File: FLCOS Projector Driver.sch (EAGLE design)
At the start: 67 parts, among them IC1 LM1117MPX-3.3, IC2 MIC5323-1.8YD5-TR, IC3 MIC5504-2.5YM5-TR, IC4 TVP5150-NTSC_DECODER, IC5 CH340G, IC6 ESP32-WROOM-32U, IC7 LM3414, IC8 LM3414, IC9 LM3414, J1 MEM2075-00-140-01-A, T1 S8050, T2 S8050, X1 14.31818MHz, X2 12MHz

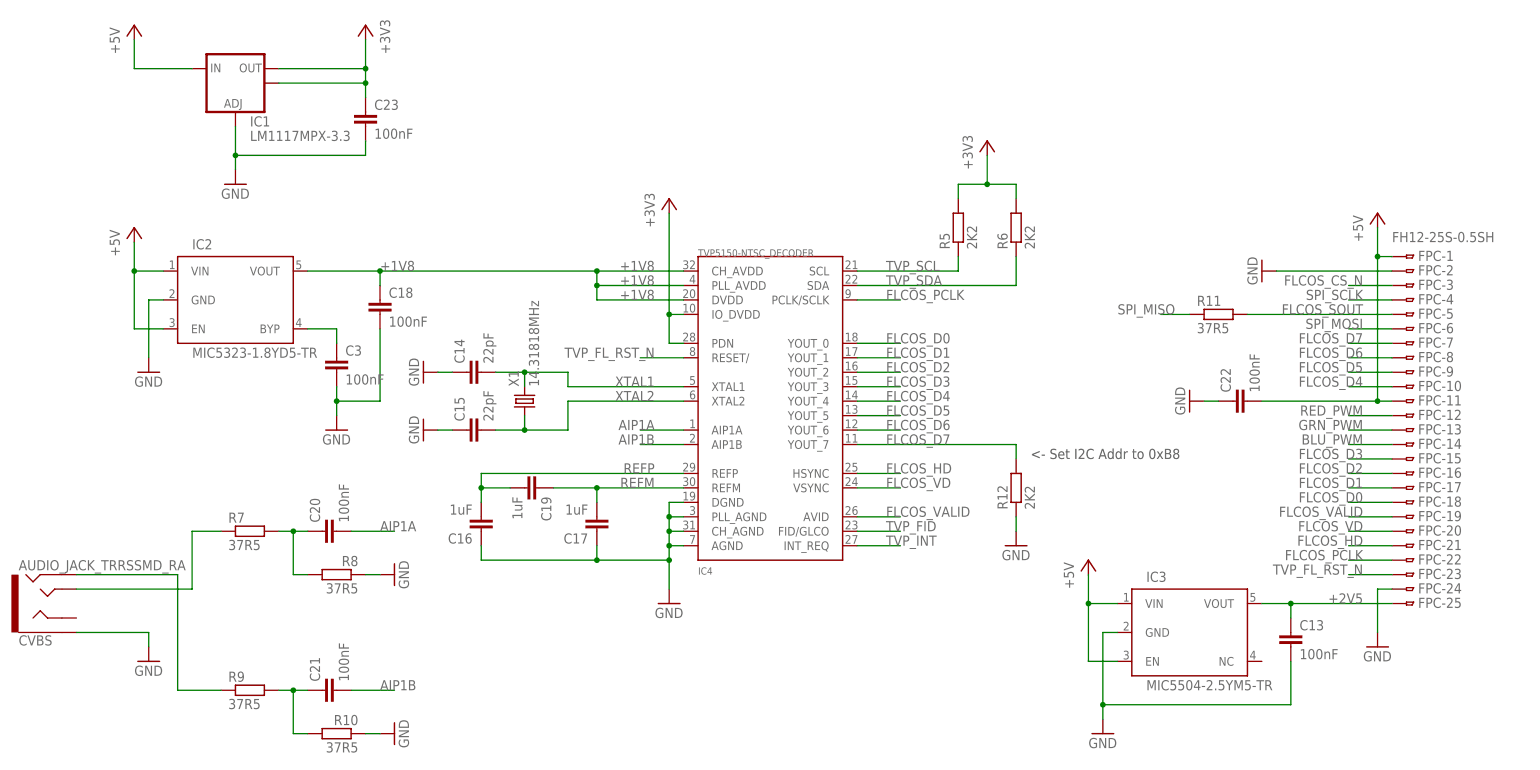
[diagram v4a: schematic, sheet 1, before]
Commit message: XLSX BOM finished. Tweaked FLCOS mounting points
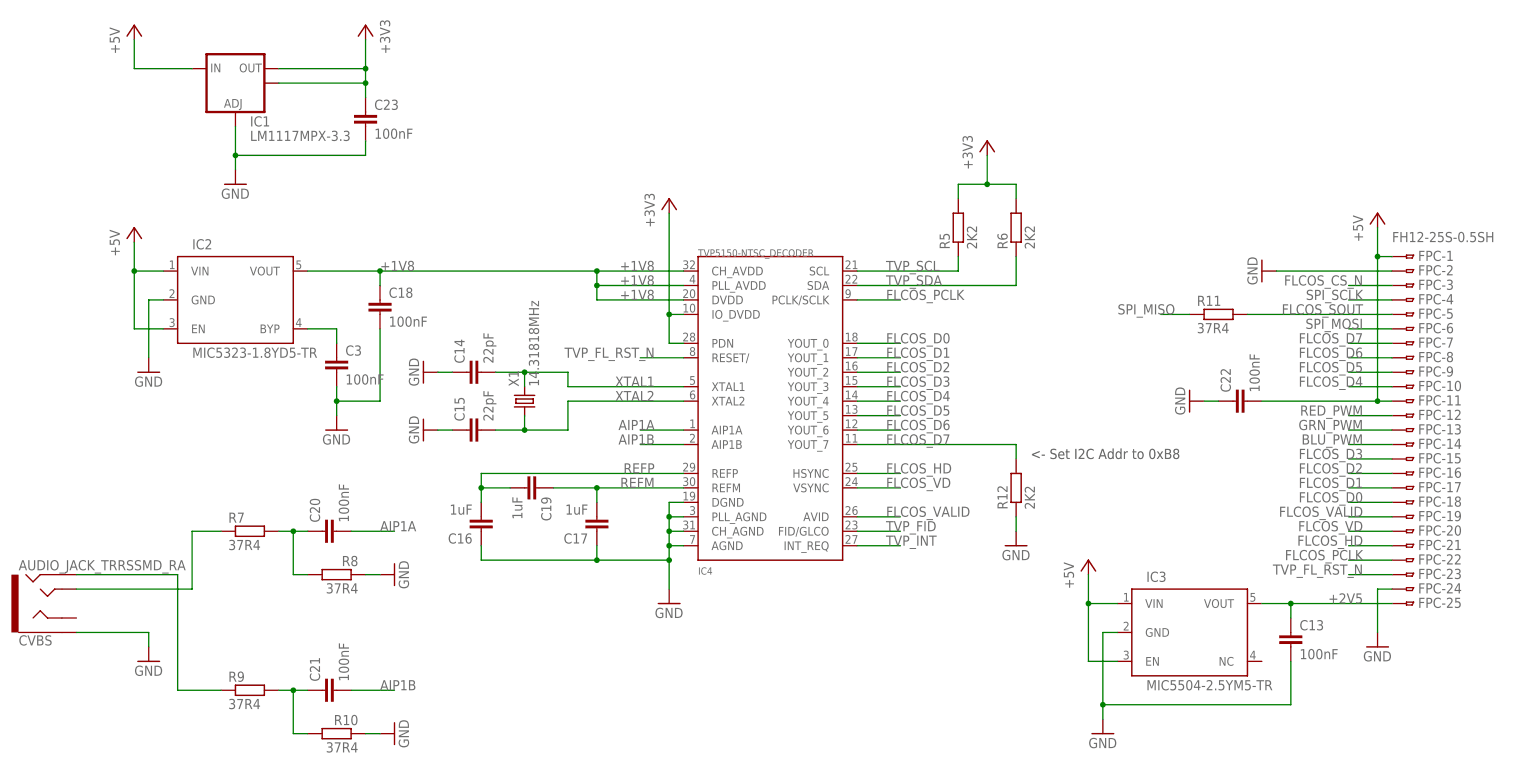
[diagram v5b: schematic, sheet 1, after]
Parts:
- R1, R15, R3: value 80K -> 82K
- R10, R11, R7, R8, R9: value 37R5 -> 37R4
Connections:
- net N$27: now also D2.A; no longer D3.A
- net N$9: now also D3.A; no longer D2.A
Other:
- moved on the sheet: D2, D3

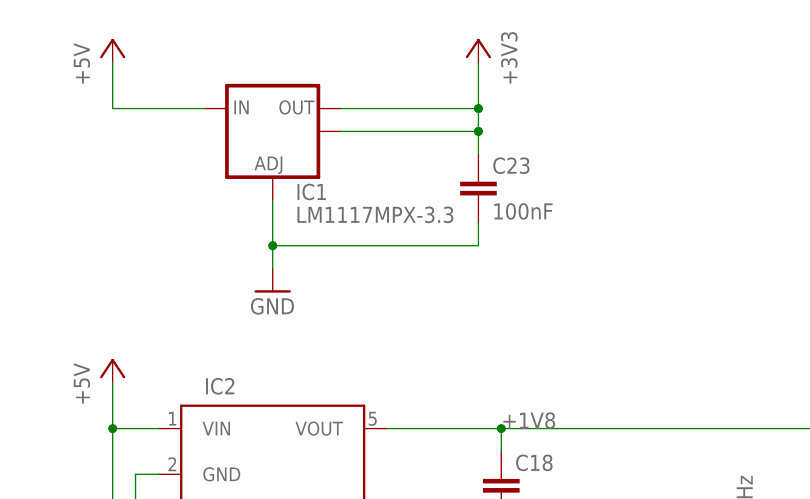
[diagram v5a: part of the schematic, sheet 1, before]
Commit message: Added Mouser cart XLS. BOM tweaks due to low stocks
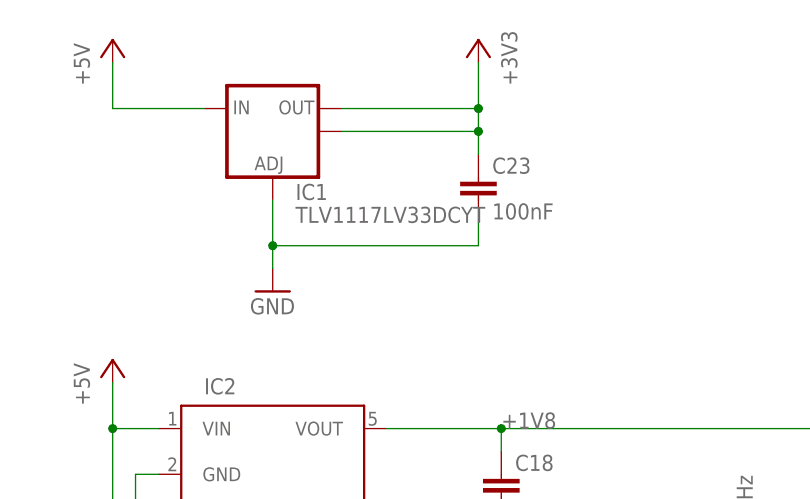
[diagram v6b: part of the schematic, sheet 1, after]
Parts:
- IC1: value LM1117MPX-3.3 -> TLV1117LV33DCYT
- IC6: value ESP32-WROOM-32U -> ESP32-WROOM-32UE-N4
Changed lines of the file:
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@@
 <part name="GND65" library="supply1" deviceset="GND" device=""/>
 <part name="U$43" library="supply1" deviceset="+3V3" device=""/>
-<part name="IC6" library="ESP32-WROOM-32U" deviceset="ESP32-WROOM-32U" device=""/>
+<part name="IC6" library="ESP32-WROOM-32U" deviceset="ESP32-WROOM-32U" device="" value="ESP32-WROOM-32UE-N4"/>
 <part name="GND66" library="supply1" deviceset="GND" device=""/>
 <part name="GND67" library="supply1" deviceset="GND" device=""/>
@@
 <part name="P+8" library="supply1" deviceset="+5V" device=""/>
 <part name="P+9" library="supply1" deviceset="+5V" device=""/>
-<part name="IC1" library="SparkFun" deviceset="V_REG_LM1117" device="SOT223" value="LM1117MPX-3.3"/>
+<part name="IC1" library="SparkFun" deviceset="V_REG_LM1117" device="SOT223" value="TLV1117LV33DCYT"/>
 <part name="RGB" library="con-jst" deviceset="ZH-8" device=""/>
 <part name="L2" library="A_butts" deviceset="INDUCTOR" device="-TAIYO-YUDEN-6X2.8" value="15uH"/>

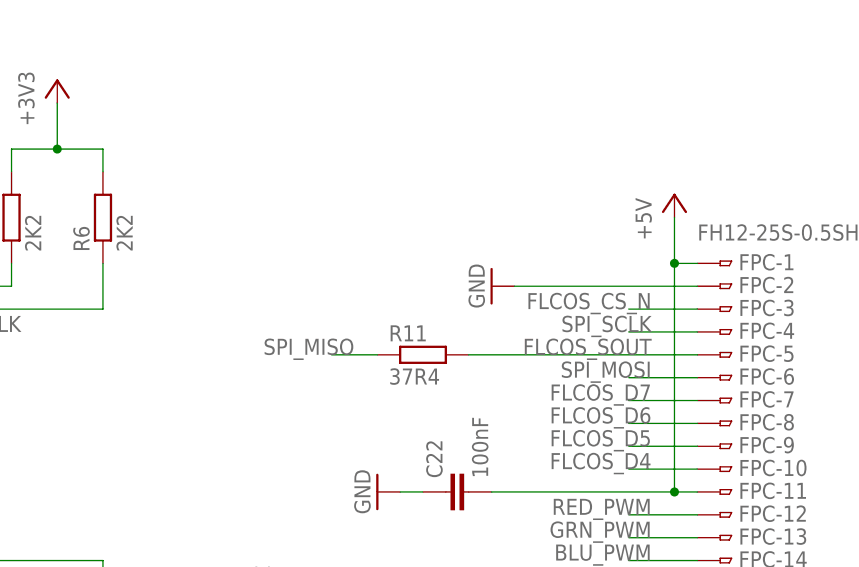
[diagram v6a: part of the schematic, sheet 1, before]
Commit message: Changed R11 to a pull-up for FLCOS_SOUT
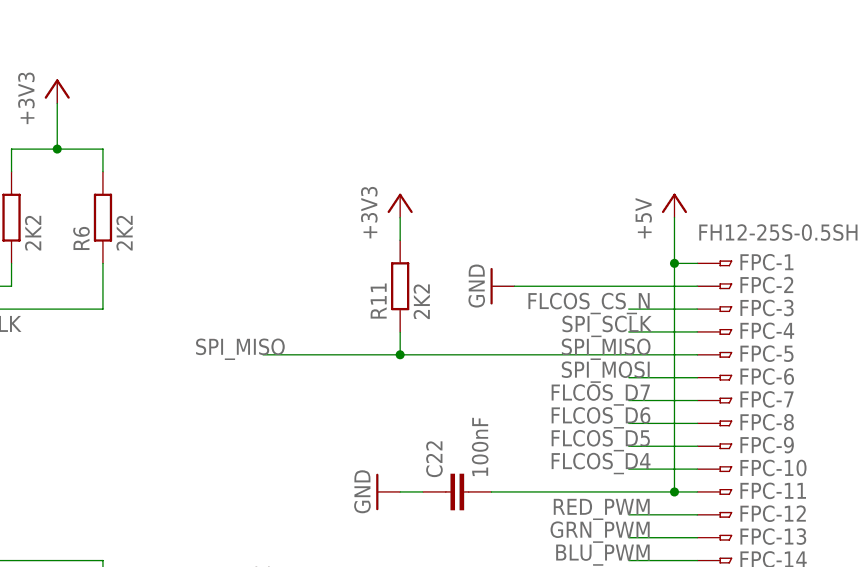
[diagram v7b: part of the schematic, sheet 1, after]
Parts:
- R11: value 37R4 -> 2K2
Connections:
- removed net FLCOS_SOUT: FPC-5.1, R11.2
- net +3V3: now also R11.2
- net SPI_MISO: now also FPC-5.1
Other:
- moved on the sheet: R11
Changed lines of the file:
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@@
 <part name="P+12" library="supply1" deviceset="+5V" device=""/>
 <part name="+3V3" library="supply1" deviceset="+3V3" device=""/>
-<part name="R11" library="rcl" deviceset="R-EU_" device="R0603" value="37R4"/>
 <part name="R5" library="rcl" deviceset="R-EU_" device="R0603" value="2K2"/>
 <part name="R6" library="rcl" deviceset="R-EU_" device="R0603" value="2K2"/>
@@
 <part name="R16" library="rcl" deviceset="R-EU_" device="R0603" value="22K"/>
 <part name="CVBS" library="SparkFun-Connectors" deviceset="AUDIO_JACK_TRRS" device="SMD_RA"/>
+<part name="R11" library="rcl" deviceset="R-EU_" device="R0603" value="2K2"/>
+<part name="+3V4" library="supply1" deviceset="+3V3" device=""/>
 </parts>
 <sheets>
@@
 <instance part="IC1" gate="G$1" x="-43.18" y="111.76"/>
 <instance part="+3V3" gate="G$1" x="88.9" y="99.06"/>
-<instance part="R11" gate="G$1" x="129.54" y="68.58"/>
 <instance part="R5" gate="G$1" x="83.82" y="83.82" rot="R90"/>
 <instance part="R6" gate="G$1" x="93.98" y="83.82" rot="R90"/>
@@
 <instance part="C3" gate="G$1" x="-25.4" y="60.96"/>
 <instance part="CVBS" gate="G$1" x="-76.2" y="17.78" rot="MR180"/>
+<instance part="R11" gate="G$1" x="127" y="76.2" rot="R90"/>
+<instance part="+3V4" gate="G$1" x="127" y="86.36"/>
 </instances>
 <busses>
@@
 </segment>
 </net>
-<net name="FLCOS_SOUT" class="0">
-<segment>
-<pinref part="FPC" gate="-5" pin="1"/>
-<label x="154.94" y="68.58" size="1.778" layer="95" rot="MR0"/>
-<wire x1="160.02" y1="68.58" x2="134.62" y2="68.58" width="0.1524" layer="91"/>
-<pinref part="R11" gate="G$1" pin="2"/>
-</segment>
-</net>
 <net name="SPI_MOSI" class="0">
 <segment>
@@
 <pinref part="R6" gate="G$1" pin="2"/>
 </segment>
+<segment>
+<pinref part="R11" gate="G$1" pin="2"/>
+<pinref part="+3V4" gate="G$1" pin="+3V3"/>
+<wire x1="127" y1="81.28" x2="127" y2="83.82" width="0.1524" layer="91"/>
+</segment>
 </net>
 <net name="TVP_FL_RST_N" class="0">
@@
 <wire x1="160.02" y1="22.86" x2="152.4" y2="22.86" width="0.1524" layer="91"/>
 <label x="154.94" y="22.86" size="1.778" layer="95" rot="MR0"/>
-</segment>
-</net>
-<net name="SPI_MISO" class="0">
-<segment>
-<wire x1="124.46" y1="68.58" x2="119.38" y2="68.58" width="0.1524" layer="91"/>
-<label x="121.92" y="68.58" size="1.778" layer="95" rot="MR0"/>
-<pinref part="R11" gate="G$1" pin="1"/>
 </segment>
 </net>
@@
 </segment>
 </net>
+<net name="SPI_MISO" class="0">
+<segment>
+<pinref part="FPC" gate="-5" pin="1"/>
+<label x="154.94" y="68.58" size="1.778" layer="95" rot="MR0"/>
+<wire x1="160.02" y1="68.58" x2="127" y2="68.58" width="0.1524" layer="91"/>
+<label x="114.3" y="68.58" size="1.778" layer="95" rot="MR0"/>
+<pinref part="R11" gate="G$1" pin="1"/>
+<wire x1="127" y1="68.58" x2="111.76" y2="68.58" width="0.1524" layer="91"/>
+<wire x1="127" y1="68.58" x2="127" y2="71.12" width="0.1524" layer="91"/>
+<junction x="127" y="68.58"/>
+</segment>
+</net>

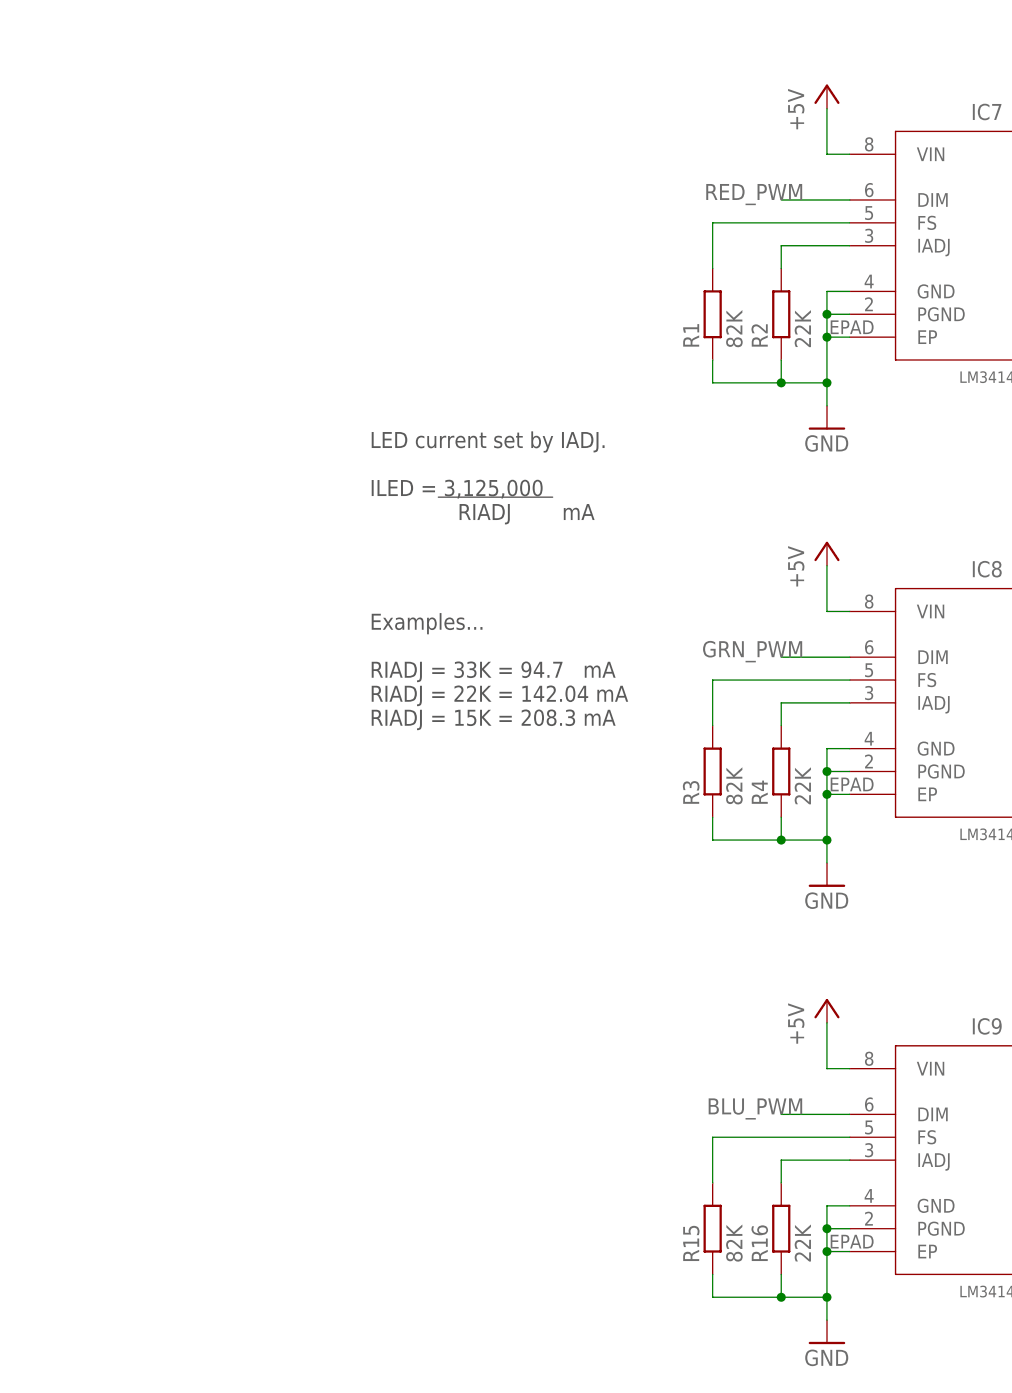
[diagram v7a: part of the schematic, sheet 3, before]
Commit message: Added inverter transistors for RGB LED PWM signals
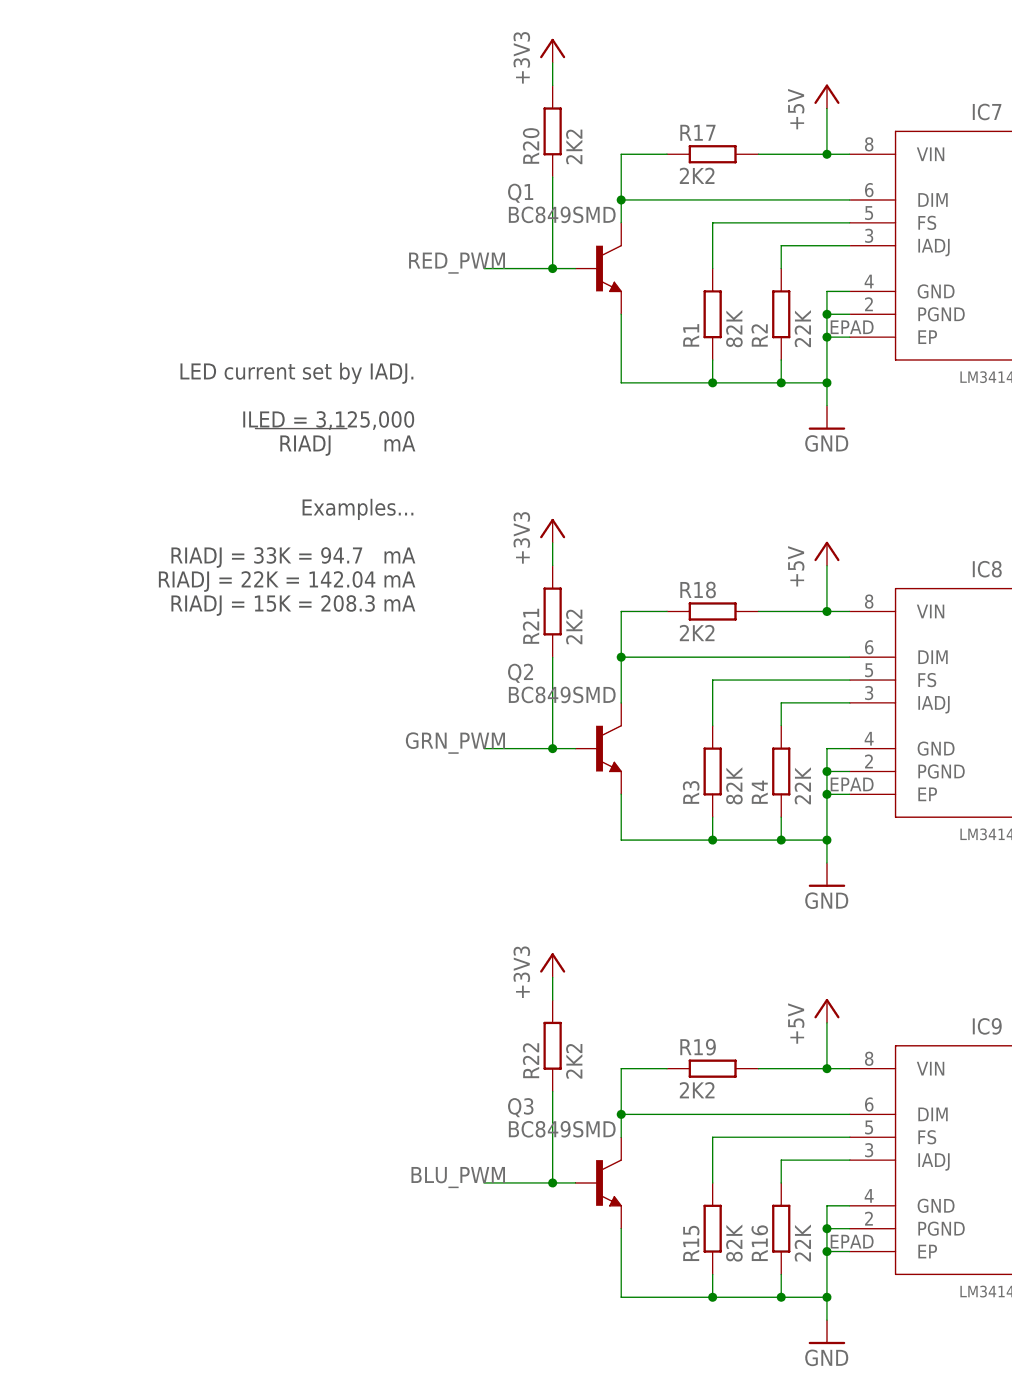
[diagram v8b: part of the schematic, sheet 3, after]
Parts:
- added C4: 100nF, rcl:C-EUC0603
- added Q1, Q2, Q3: BC849SMD, transistor-npn:BC849SMD
- added R17, R18, R19, R20, R21, R22: 2K2, rcl:R-EU_R0603
- R67: value 2K2 -> 12K
- T1, T2: device transistor:BC846 -> transistor-npn:BC849SMD
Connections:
- new net N$1: IC7.DIM, Q1.C, R17.1
- new net N$11: IC8.DIM, Q2.C, R18.1
- new net N$12: IC9.DIM, Q3.C, R19.1
- net +3V3: now also R20.2, R21.2, R22.2
- net +5V: now also R17.2, R18.2, R19.2
- net BLU_PWM: now also Q3.B, R22.1; no longer IC9.DIM
- net ESP_EN_N: now also C4.2
- net GND: now also C4.1, Q1.E, Q2.E, Q3.E
- net GRN_PWM: now also Q2.B, R21.1; no longer IC8.DIM
- net N$67: now also IC5.TXD; no longer IC5.TX
- net N$70: now also IC5.RXD; no longer IC5.RX
- net N$78: now also IC5.RTS_N; no longer IC5.RTS
- net N$79: now also IC5.DTR_N; no longer IC5.DTR
- net RED_PWM: now also Q1.B, R20.1; no longer IC7.DIM
